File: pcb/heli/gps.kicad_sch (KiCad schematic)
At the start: 1 part

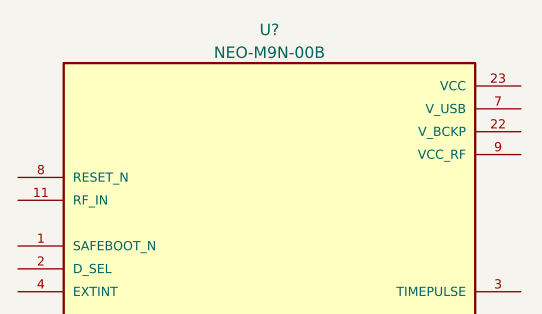
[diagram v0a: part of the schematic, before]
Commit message: 
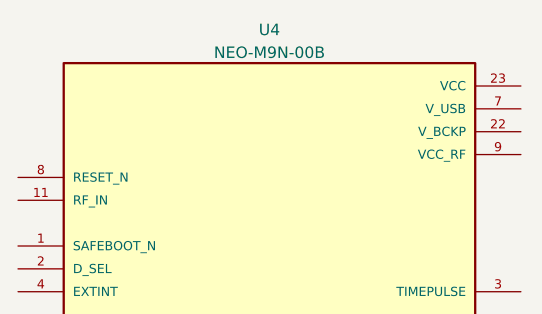
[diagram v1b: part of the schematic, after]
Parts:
- gave numbers to parts that had none: 1
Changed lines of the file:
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@@
   (symbol (lib_id "ICs:NEO-M9N-00B") (at 155.575 90.805 0) (unit 1)
     (in_bom yes) (on_board yes) (fields_autoplaced)
-    (property "Reference" "U?" (id 0) (at 155.575 59.1652 0))
+    (property "Reference" "U4" (id 0) (at 155.575 59.1652 0))
     (property "Value" "NEO-M9N-00B" (id 1) (at 155.575 61.7021 0))
     (property "Footprint" "ICs:XCVR_NEO-M9N-00B" (id 2) (at 155.575 90.805 0)

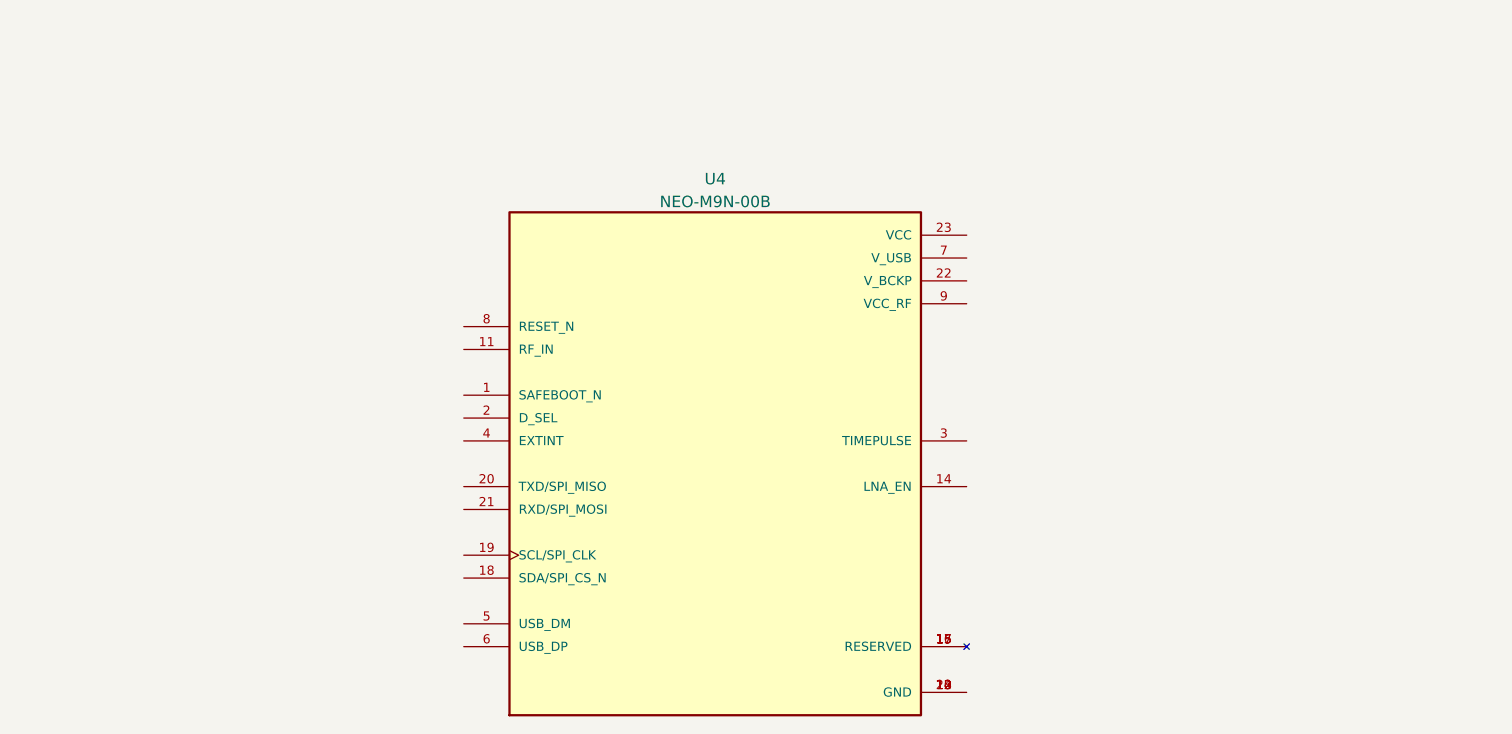
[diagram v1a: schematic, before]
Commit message: 
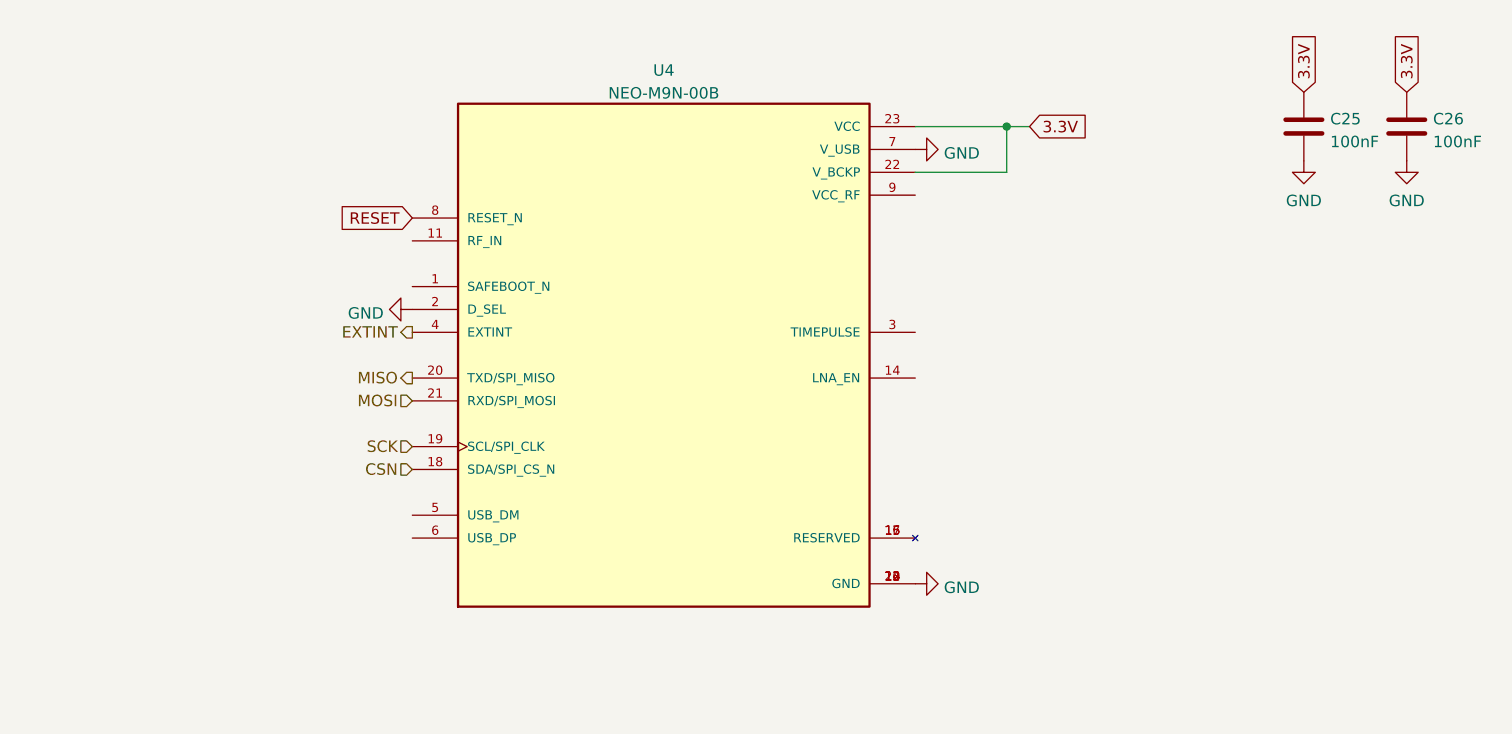
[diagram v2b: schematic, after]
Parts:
- added C25, C26: 100nF, Capacitor_SMD:C_0603_1608Metric, symbol Device:C
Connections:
- net GND: now reaches U4.10 (GND), U4.12 (GND), U4.13 (GND), U4.24 (GND)
- net GND: now also U4.2 (D_SEL), U4.7 (V_USB), C25.2, C26.2
- net CSN: now reaches U4.18 (SDA/SPI_CS_N)
- net SCK: now reaches U4.19 (SCL/SPI_CLK)
- net MISO: now reaches U4.20 (TXD/SPI_MISO)
- net MOSI: now reaches U4.21 (RXD/SPI_MOSI)
- net 3.3V: now reaches U4.22 (V_BCKP)
- net 3.3V: now also U4.23 (VCC), C25.1, C26.1
- net EXTINT: now reaches U4.4 (EXTINT)
- net RESET: now reaches U4.8 (RESET_N)
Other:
- moved on the sheet: U4
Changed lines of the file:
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@@
 (kicad_sch (version 20211123) (generator eeschema)
   (paper "A4")
-  (symbol (lib_id "ICs:NEO-M9N-00B") (at 155.575 90.805 0) (unit 1)
-    (in_bom yes) (on_board yes) (fields_autoplaced)
-    (property "Reference" "U4" (id 0) (at 155.575 59.1652 0))
-    (property "Value" "NEO-M9N-00B" (id 1) (at 155.575 61.7021 0))
-    (property "Footprint" "ICs:XCVR_NEO-M9N-00B" (id 2) (at 155.575 90.805 0)
-      (effects (font (size 1.27 1.27)) (justify bottom) hide)
-    )
-    (property "Datasheet" "" (id 3) (at 155.575 90.805 0)
-      (effects (font (size 1.27 1.27)) hide)
-    )
-    (property "STANDARD" "Manufacturer Recommendations" (id 4) (at 155.575 90.805 0)
-      (effects (font (size 1.27 1.27)) (justify bottom) hide)
-    )
-    (property "MAXIMUM_PACKAGE_HEIGHT" "2.6mm" (id 5) (at 155.575 90.805 0)
-      (effects (font (size 1.27 1.27)) (justify bottom) hide)
-    )
-    (property "MANUFACTURER" "U blox" (id 6) (at 155.575 90.805 0)
-      (effects (font (size 1.27 1.27)) (justify bottom) hide)
-    )
-    (property "PARTREV" "R05" (id 7) (at 155.575 90.805 0)
+  (junction (at 187.96 53.34) (diameter 0) (color 0 0 0 0)
+  )
+  (wire (pts (xy 190.5 53.34) (xy 187.96 53.34))
+    (stroke (width 0) (type default) (color 0 0 0 0))
+  )
+  (wire (pts (xy 177.8 58.42) (xy 187.96 58.42))
+    (stroke (width 0) (type default) (color 0 0 0 0))
+  )
+  (wire (pts (xy 177.8 53.34) (xy 187.96 53.34))
+    (stroke (width 0) (type default) (color 0 0 0 0))
+  )
+  (wire (pts (xy 187.96 58.42) (xy 187.96 53.34))
+    (stroke (width 0) (type default) (color 0 0 0 0))
+  )
+  (global_label "3.3V" (shape input) (at 190.5 53.34 0) (fields_autoplaced)
+    (effects (font (size 1.27 1.27)) (justify left))
+    (property "Intersheet References" "${INTERSHEET_REFS}" (id 0) (at 197.0255 53.2606 0)
+      (effects (font (size 1.27 1.27)) (justify left) hide)
+    )
+  )
+  (global_label "3.3V" (shape input) (at 232.41 49.53 90) (fields_autoplaced)
+    (effects (font (size 1.27 1.27)) (justify left))
+    (property "Intersheet References" "${INTERSHEET_REFS}" (id 0) (at 232.3306 43.0045 90)
+      (effects (font (size 1.27 1.27)) (justify left) hide)
+    )
+  )
+  (global_label "RESET" (shape input) (at 121.92 63.5 180) (fields_autoplaced)
+    (effects (font (size 1.27 1.27)) (justify right))
+    (property "Intersheet References" "${INTERSHEET_REFS}" (id 0) (at 113.7617 63.4206 0)
+      (effects (font (size 1.27 1.27)) (justify right) hide)
+    )
+  )
+  (global_label "3.3V" (shape input) (at 220.98 49.53 90) (fields_autoplaced)
+    (effects (font (size 1.27 1.27)) (justify left))
+    (property "Intersheet References" "${INTERSHEET_REFS}" (id 0) (at 220.9006 43.0045 90)
+      (effects (font (size 1.27 1.27)) (justify left) hide)
+    )
+  )
+  (hierarchical_label "CSN" (shape input) (at 121.92 91.44 180)
+    (effects (font (size 1.27 1.27)) (justify right))
+  )
+  (hierarchical_label "SCK" (shape input) (at 121.92 88.9 180)
+    (effects (font (size 1.27 1.27)) (justify right))
+  )
+  (hierarchical_label "EXTINT" (shape output) (at 121.92 76.2 180)
+    (effects (font (size 1.27 1.27)) (justify right))
+  )
+  (hierarchical_label "MISO" (shape output) (at 121.92 81.28 180)
+    (effects (font (size 1.27 1.27)) (justify right))
+  )
+  (hierarchical_label "MOSI" (shape input) (at 121.92 83.82 180)
+    (effects (font (size 1.27 1.27)) (justify right))
+  )
+  (symbol (lib_id "Device:C") (at 232.41 53.34 0) (unit 1)
+    (in_bom yes) (on_board yes) (fields_autoplaced)
+    (property "Reference" "C26" (id 0) (at 235.331 52.5053 0)
+      (effects (font (size 1.27 1.27)) (justify left))
+    )
+    (property "Value" "100nF" (id 1) (at 235.331 55.0422 0)
+      (effects (font (size 1.27 1.27)) (justify left))
+    )
+    (property "Footprint" "Capacitor_SMD:C_0603_1608Metric" (id 2) (at 233.3752 57.15 0)
+      (effects (font (size 1.27 1.27)) hide)
+    )
+    (property "Datasheet" "~" (id 3) (at 232.41 53.34 0)
+      (effects (font (size 1.27 1.27)) hide)
+    )
+    (pin "1")
+    (pin "2")
+  )
+  (symbol (lib_id "power:GND") (at 220.98 57.15 0) (unit 1)
+    (in_bom yes) (on_board yes) (fields_autoplaced)
+    (property "Reference" "#PWR0117" (id 0) (at 220.98 63.5 0)
+      (effects (font (size 1.27 1.27)) hide)
+    )
+    (property "Value" "GND" (id 1) (at 220.98 61.5934 0))
+    (property "Footprint" "" (id 2) (at 220.98 57.15 0)
+      (effects (font (size 1.27 1.27)) hide)
+    )
+    (property "Datasheet" "" (id 3) (at 220.98 57.15 0)
+      (effects (font (size 1.27 1.27)) hide)
+    )
+    (pin "1")
+  )
+  (symbol (lib_id "Device:C") (at 220.98 53.34 0) (unit 1)
+    (in_bom yes) (on_board yes) (fields_autoplaced)
+    (property "Reference" "C25" (id 0) (at 223.901 52.5053 0)
+      (effects (font (size 1.27 1.27)) (justify left))
+    )
+    (property "Value" "100nF" (id 1) (at 223.901 55.0422 0)
+      (effects (font (size 1.27 1.27)) (justify left))
+    )
+    (property "Footprint" "Capacitor_SMD:C_0603_1608Metric" (id 2) (at 221.9452 57.15 0)
+      (effects (font (size 1.27 1.27)) hide)
+    )
+    (property "Datasheet" "~" (id 3) (at 220.98 53.34 0)
+      (effects (font (size 1.27 1.27)) hide)
+    )
+    (pin "1")
+    (pin "2")
+  )
+  (symbol (lib_id "power:GND") (at 121.92 73.66 270) (unit 1)
+    (in_bom yes) (on_board yes) (fields_autoplaced)
+    (property "Reference" "#PWR0114" (id 0) (at 115.57 73.66 0)
+      (effects (font (size 1.27 1.27)) hide)
+    )
+    (property "Value" "GND" (id 1) (at 118.7451 74.0938 90)
+      (effects (font (size 1.27 1.27)) (justify right))
+    )
+    (property "Footprint" "" (id 2) (at 121.92 73.66 0)
+      (effects (font (size 1.27 1.27)) hide)
+    )
+    (property "Datasheet" "" (id 3) (at 121.92 73.66 0)
+      (effects (font (size 1.27 1.27)) hide)
+    )
+    (pin "1")
+  )
+  (symbol (lib_id "ICs:NEO-M9N-00B") (at 149.86 78.74 0) (unit 1)
+    (in_bom yes) (on_board yes) (fields_autoplaced)
+    (property "Reference" "U4" (id 0) (at 149.86 47.1002 0))
+    (property "Value" "NEO-M9N-00B" (id 1) (at 149.86 49.6371 0))
+    (property "Footprint" "ICs:XCVR_NEO-M9N-00B" (id 2) (at 149.86 78.74 0)
+      (effects (font (size 1.27 1.27)) (justify bottom) hide)
+    )
+    (property "Datasheet" "" (id 3) (at 149.86 78.74 0)
+      (effects (font (size 1.27 1.27)) hide)
+    )
+    (property "STANDARD" "Manufacturer Recommendations" (id 4) (at 149.86 78.74 0)
+      (effects (font (size 1.27 1.27)) (justify bottom) hide)
+    )
+    (property "MAXIMUM_PACKAGE_HEIGHT" "2.6mm" (id 5) (at 149.86 78.74 0)
+      (effects (font (size 1.27 1.27)) (justify bottom) hide)
+    )
+    (property "MANUFACTURER" "U blox" (id 6) (at 149.86 78.74 0)
+      (effects (font (size 1.27 1.27)) (justify bottom) hide)
+    )
+    (property "PARTREV" "R05" (id 7) (at 149.86 78.74 0)
       (effects (font (size 1.27 1.27)) (justify bottom) hide)
     )
@@
     (pin "9")
   )
+  (symbol (lib_id "power:GND") (at 177.8 55.88 90) (unit 1)
+    (in_bom yes) (on_board yes) (fields_autoplaced)
+    (property "Reference" "#PWR0115" (id 0) (at 184.15 55.88 0)
+      (effects (font (size 1.27 1.27)) hide)
+    )
+    (property "Value" "GND" (id 1) (at 180.975 56.3138 90)
+      (effects (font (size 1.27 1.27)) (justify right))
+    )
+    (property "Footprint" "" (id 2) (at 177.8 55.88 0)
+      (effects (font (size 1.27 1.27)) hide)
+    )
+    (property "Datasheet" "" (id 3) (at 177.8 55.88 0)
+      (effects (font (size 1.27 1.27)) hide)
+    )
+    (pin "1")
+  )
+  (symbol (lib_id "power:GND") (at 232.41 57.15 0) (unit 1)
+    (in_bom yes) (on_board yes) (fields_autoplaced)
+    (property "Reference" "#PWR0118" (id 0) (at 232.41 63.5 0)
+      (effects (font (size 1.27 1.27)) hide)
+    )
+    (property "Value" "GND" (id 1) (at 232.41 61.5934 0))
+    (property "Footprint" "" (id 2) (at 232.41 57.15 0)
+      (effects (font (size 1.27 1.27)) hide)
+    )
+    (property "Datasheet" "" (id 3) (at 232.41 57.15 0)
+      (effects (font (size 1.27 1.27)) hide)
+    )
+    (pin "1")
+  )
+  (symbol (lib_id "power:GND") (at 177.8 104.14 90) (unit 1)
+    (in_bom yes) (on_board yes) (fields_autoplaced)
+    (property "Reference" "#PWR0116" (id 0) (at 184.15 104.14 0)
+      (effects (font (size 1.27 1.27)) hide)
+    )
+    (property "Value" "GND" (id 1) (at 180.975 104.5738 90)
+      (effects (font (size 1.27 1.27)) (justify right))
+    )
+    (property "Footprint" "" (id 2) (at 177.8 104.14 0)
+      (effects (font (size 1.27 1.27)) hide)
+    )
+    (property "Datasheet" "" (id 3) (at 177.8 104.14 0)
+      (effects (font (size 1.27 1.27)) hide)
+    )
+    (pin "1")
+  )
 )

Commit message: 
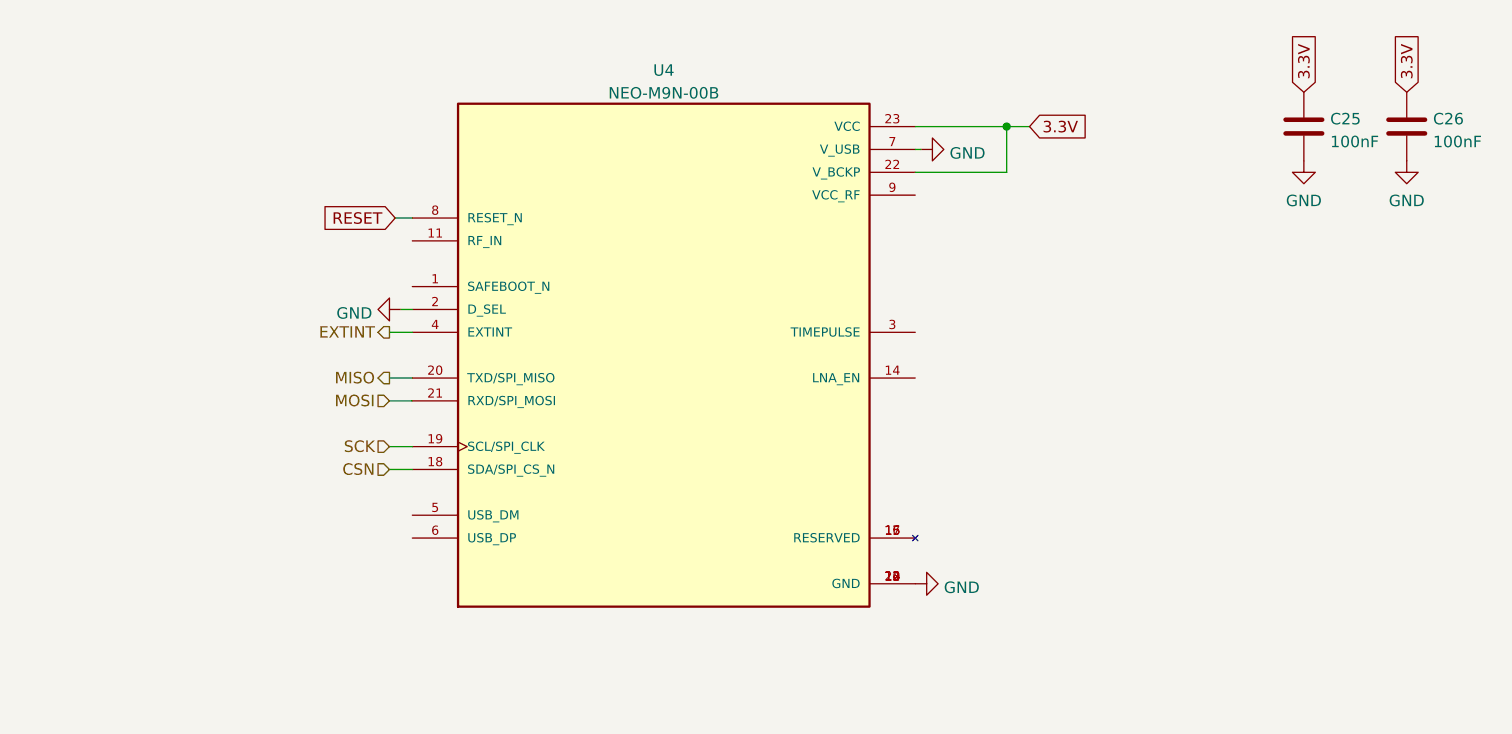
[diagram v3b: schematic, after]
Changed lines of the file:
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@@
   (junction (at 187.96 53.34) (diameter 0) (color 0 0 0 0)
   )
+  (wire (pts (xy 119.38 91.44) (xy 121.92 91.44))
+    (stroke (width 0) (type default) (color 0 0 0 0))
+  )
+  (wire (pts (xy 119.38 83.82) (xy 121.92 83.82))
+    (stroke (width 0) (type default) (color 0 0 0 0))
+  )
   (wire (pts (xy 190.5 53.34) (xy 187.96 53.34))
     (stroke (width 0) (type default) (color 0 0 0 0))
   )
+  (wire (pts (xy 119.38 88.9) (xy 121.92 88.9))
+    (stroke (width 0) (type default) (color 0 0 0 0))
+  )
   (wire (pts (xy 177.8 58.42) (xy 187.96 58.42))
     (stroke (width 0) (type default) (color 0 0 0 0))
   )
+  (wire (pts (xy 119.38 76.2) (xy 121.92 76.2))
+    (stroke (width 0) (type default) (color 0 0 0 0))
+  )
+  (wire (pts (xy 120.015 63.5) (xy 121.92 63.5))
+    (stroke (width 0) (type default) (color 0 0 0 0))
+  )
   (wire (pts (xy 177.8 53.34) (xy 187.96 53.34))
+    (stroke (width 0) (type default) (color 0 0 0 0))
+  )
+  (wire (pts (xy 119.38 81.28) (xy 121.92 81.28))
+    (stroke (width 0) (type default) (color 0 0 0 0))
+  )
+  (wire (pts (xy 120.65 73.66) (xy 121.92 73.66))
+    (stroke (width 0) (type default) (color 0 0 0 0))
+  )
+  (wire (pts (xy 178.435 55.88) (xy 177.8 55.88))
     (stroke (width 0) (type default) (color 0 0 0 0))
   )
@@
     )
   )
-  (global_label "RESET" (shape input) (at 121.92 63.5 180) (fields_autoplaced)
-    (effects (font (size 1.27 1.27)) (justify right))
-    (property "Intersheet References" "${INTERSHEET_REFS}" (id 0) (at 113.7617 63.4206 0)
+  (global_label "RESET" (shape input) (at 120.015 63.5 180) (fields_autoplaced)
+    (effects (font (size 1.27 1.27)) (justify right))
+    (property "Intersheet References" "${INTERSHEET_REFS}" (id 0) (at 111.8567 63.4206 0)
       (effects (font (size 1.27 1.27)) (justify right) hide)
     )
@@
     )
   )
-  (hierarchical_label "CSN" (shape input) (at 121.92 91.44 180)
-    (effects (font (size 1.27 1.27)) (justify right))
-  )
-  (hierarchical_label "SCK" (shape input) (at 121.92 88.9 180)
-    (effects (font (size 1.27 1.27)) (justify right))
-  )
-  (hierarchical_label "EXTINT" (shape output) (at 121.92 76.2 180)
-    (effects (font (size 1.27 1.27)) (justify right))
-  )
-  (hierarchical_label "MISO" (shape output) (at 121.92 81.28 180)
-    (effects (font (size 1.27 1.27)) (justify right))
-  )
-  (hierarchical_label "MOSI" (shape input) (at 121.92 83.82 180)
+  (hierarchical_label "CSN" (shape input) (at 119.38 91.44 180)
+    (effects (font (size 1.27 1.27)) (justify right))
+  )
+  (hierarchical_label "SCK" (shape input) (at 119.38 88.9 180)
+    (effects (font (size 1.27 1.27)) (justify right))
+  )
+  (hierarchical_label "EXTINT" (shape output) (at 119.38 76.2 180)
+    (effects (font (size 1.27 1.27)) (justify right))
+  )
+  (hierarchical_label "MISO" (shape output) (at 119.38 81.28 180)
+    (effects (font (size 1.27 1.27)) (justify right))
+  )
+  (hierarchical_label "MOSI" (shape input) (at 119.38 83.82 180)
     (effects (font (size 1.27 1.27)) (justify right))
   )
@@
     (pin "2")
   )
-  (symbol (lib_id "power:GND") (at 121.92 73.66 270) (unit 1)
-    (in_bom yes) (on_board yes) (fields_autoplaced)
-    (property "Reference" "#PWR0114" (id 0) (at 115.57 73.66 0)
-      (effects (font (size 1.27 1.27)) hide)
-    )
-    (property "Value" "GND" (id 1) (at 118.7451 74.0938 90)
+  (symbol (lib_id "power:GND") (at 120.65 73.66 270) (unit 1)
+    (in_bom yes) (on_board yes) (fields_autoplaced)
+    (property "Reference" "#PWR0114" (id 0) (at 114.3 73.66 0)
+      (effects (font (size 1.27 1.27)) hide)
+    )
+    (property "Value" "GND" (id 1) (at 117.4751 74.0938 90)
       (effects (font (size 1.27 1.27)) (justify right))
     )
-    (property "Footprint" "" (id 2) (at 121.92 73.66 0)
-      (effects (font (size 1.27 1.27)) hide)
-    )
-    (property "Datasheet" "" (id 3) (at 121.92 73.66 0)
+    (property "Footprint" "" (id 2) (at 120.65 73.66 0)
+      (effects (font (size 1.27 1.27)) hide)
+    )
+    (property "Datasheet" "" (id 3) (at 120.65 73.66 0)
       (effects (font (size 1.27 1.27)) hide)
     )
@@
     (pin "9")
   )
-  (symbol (lib_id "power:GND") (at 177.8 55.88 90) (unit 1)
-    (in_bom yes) (on_board yes) (fields_autoplaced)
-    (property "Reference" "#PWR0115" (id 0) (at 184.15 55.88 0)
-      (effects (font (size 1.27 1.27)) hide)
-    )
-    (property "Value" "GND" (id 1) (at 180.975 56.3138 90)
+  (symbol (lib_id "power:GND") (at 178.435 55.88 90) (unit 1)
+    (in_bom yes) (on_board yes) (fields_autoplaced)
+    (property "Reference" "#PWR0115" (id 0) (at 184.785 55.88 0)
+      (effects (font (size 1.27 1.27)) hide)
+    )
+    (property "Value" "GND" (id 1) (at 181.61 56.3138 90)
       (effects (font (size 1.27 1.27)) (justify right))
     )
-    (property "Footprint" "" (id 2) (at 177.8 55.88 0)
-      (effects (font (size 1.27 1.27)) hide)
-    )
-    (property "Datasheet" "" (id 3) (at 177.8 55.88 0)
-      (effects (font (size 1.27 1.27)) hide)
-    )
+    (property "Footprint" "" (id 2) (at 178.435 55.88 0)
+      (effects (font (size 1.27 1.27)) hide)
+    )
+    (property "Datasheet" "" (id 3) (at 178.435 55.88 0)
+      (effects (font (size 1.27 1.27)) hide)
+    )
